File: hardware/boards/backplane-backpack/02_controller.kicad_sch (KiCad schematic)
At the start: 4 parts, among them J10 SWD, U1 STM32C092FCP6

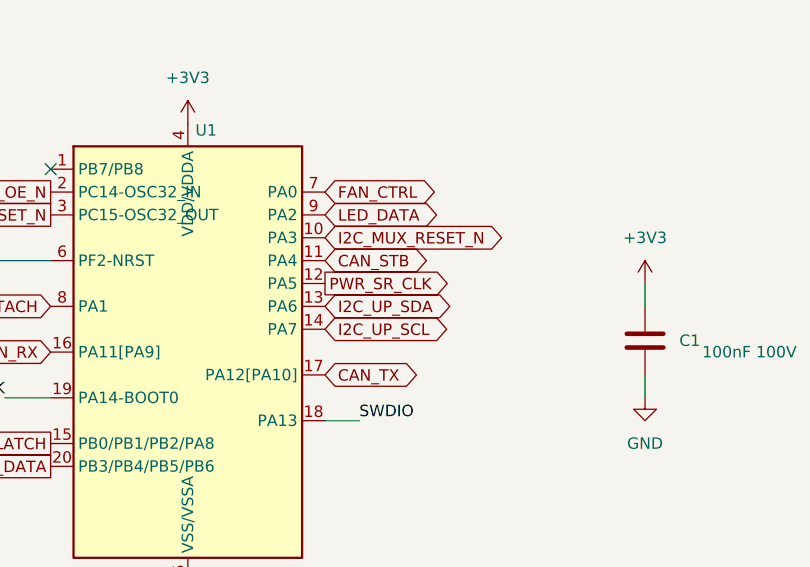
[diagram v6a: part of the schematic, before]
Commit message: feat: replicate slot power switch layouts
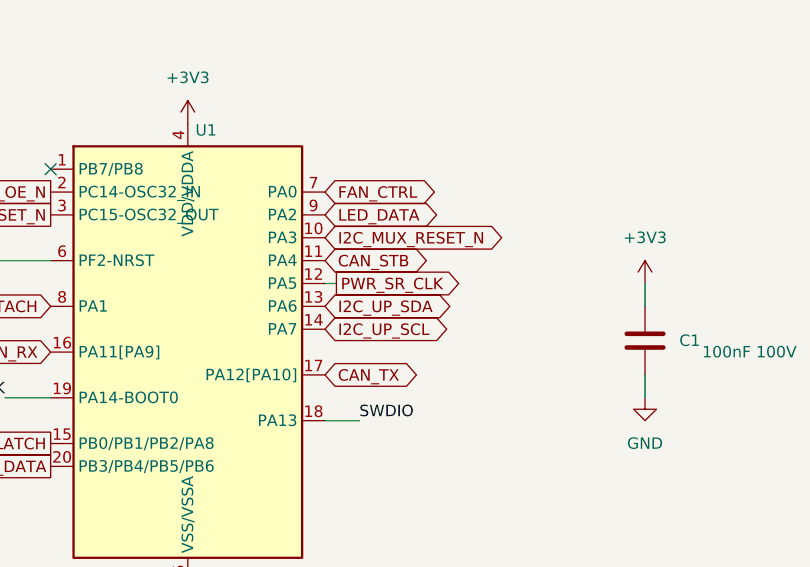
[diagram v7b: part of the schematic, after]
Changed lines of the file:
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@@
+	(wire
+		(pts
+			(xy 118.11 93.98) (xy 116.84 93.98)
+		)
+		(stroke
+			(width 0)
+			(type default)
+		)
+	)
 	(wire
 		(pts
@@
 			)
 			(justify left bottom)
+		)
+	)
+	(global_label "I2C_UP_SCL"
+		(shape bidirectional)
+		(at 116.84 99.06 0)
+		(effects
+			(font
+				(size 1.27 1.27)
+			)
+			(justify left)
+		)
+		(property "Intersheetrefs" "${INTERSHEET_REFS}"
+			(at 116.84 99.06 0)
+			(hide yes)
+			(show_name no)
+			(do_not_autoplace no)
+			(effects
+				(font
+					(size 1.27 1.27)
+				)
+			)
+		)
+	)
+	(global_label "PWR_SR_CLK"
+		(shape output)
+		(at 118.11 93.98 0)
+		(effects
+			(font
+				(size 1.27 1.27)
+			)
+			(justify left)
+		)
+		(property "Intersheetrefs" "${INTERSHEET_REFS}"
+			(at 118.11 93.98 0)
+			(hide yes)
+			(show_name no)
+			(do_not_autoplace no)
+			(effects
+				(font
+					(size 1.27 1.27)
+				)
+			)
+		)
+	)
+	(global_label "I2C_MUX_RESET_N"
+		(shape bidirectional)
+		(at 116.84 88.9 0)
+		(effects
+			(font
+				(size 1.27 1.27)
+			)
+			(justify left)
+		)
+		(property "Intersheetrefs" "${INTERSHEET_REFS}"
+			(at 116.84 88.9 0)
+			(hide yes)
+			(show_name no)
+			(do_not_autoplace no)
+			(effects
+				(font
+					(size 1.27 1.27)
+				)
+			)
+		)
+	)
+	(global_label "I2C_UP_SDA"
+		(shape bidirectional)
+		(at 116.84 96.52 0)
+		(effects
+			(font
+				(size 1.27 1.27)
+			)
+			(justify left)
+		)
+		(property "Intersheetrefs" "${INTERSHEET_REFS}"
+			(at 116.84 96.52 0)
+			(hide yes)
+			(show_name no)
+			(do_not_autoplace no)
+			(effects
+				(font
+					(size 1.27 1.27)
+				)
+			)
 		)
 	)
@@
 		)
 	)
+	(global_label "CAN_RX"
+		(shape bidirectional)
+		(at 86.36 101.6 180)
+		(effects
+			(font
+				(size 1.27 1.27)
+			)
+			(justify right)
+		)
+		(property "Intersheetrefs" "${INTERSHEET_REFS}"
+			(at 86.36 101.6 0)
+			(hide yes)
+			(show_name no)
+			(do_not_autoplace no)
+			(effects
+				(font
+					(size 1.27 1.27)
+				)
+			)
+		)
+	)
 	(global_label "PWR_SR_RESET_N"
 		(shape output)
@@
 		)
 	)
+	(global_label "PWR_SR_CLK"
+		(shape bidirectional)
+		(at 25.4 63.5 0)
+		(effects
+			(font
+				(size 1.27 1.27)
+			)
+			(justify left)
+		)
+		(property "Intersheetrefs" "${INTERSHEET_REFS}"
+			(at 25.4 63.5 0)
+			(hide yes)
+			(show_name no)
+			(do_not_autoplace no)
+			(effects
+				(font
+					(size 1.27 1.27)
+				)
+			)
+		)
+	)
+	(global_label "CAN_STB"
+		(shape bidirectional)
+		(at 116.84 91.44 0)
+		(effects
+			(font
+				(size 1.27 1.27)
+			)
+			(justify left)
+		)
+		(property "Intersheetrefs" "${INTERSHEET_REFS}"
+			(at 116.84 91.44 0)
+			(hide yes)
+			(show_name no)
+			(do_not_autoplace no)
+			(effects
+				(font
+					(size 1.27 1.27)
+				)
+			)
+		)
+	)
+	(global_label "FAN_TACH"
+		(shape bidirectional)
+		(at 86.36 96.52 180)
+		(effects
+			(font
+				(size 1.27 1.27)
+			)
+			(justify right)
+		)
+		(property "Intersheetrefs" "${INTERSHEET_REFS}"
+			(at 86.36 96.52 0)
+			(hide yes)
+			(show_name no)
+			(do_not_autoplace no)
+			(effects
+				(font
+					(size 1.27 1.27)
+				)
+			)
+		)
+	)
+	(global_label "CAN_TX"
+		(shape bidirectional)
+		(at 116.84 104.14 0)
+		(effects
+			(font
+				(size 1.27 1.27)
+			)
+			(justify left)
+		)
+		(property "Intersheetrefs" "${INTERSHEET_REFS}"
+			(at 116.84 104.14 0)
+			(hide yes)
+			(show_name no)
+			(do_not_autoplace no)
+			(effects
+				(font
+					(size 1.27 1.27)
+				)
+			)
+		)
+	)
+	(global_label "LED_DATA"
+		(shape bidirectional)
+		(at 116.84 86.36 0)
+		(effects
+			(font
+				(size 1.27 1.27)
+			)
+			(justify left)
+		)
+		(property "Intersheetrefs" "${INTERSHEET_REFS}"
+			(at 116.84 86.36 0)
+			(hide yes)
+			(show_name no)
+			(do_not_autoplace no)
+			(effects
+				(font
+					(size 1.27 1.27)
+				)
+			)
+		)
+	)
 	(global_label "PWR_SR_DATA"
 		(shape output)
@@
 			(hide yes)
 			(show_name no)
-			(do_not_autoplace no)
-			(effects
-				(font
-					(size 1.27 1.27)
-				)
-			)
-		)
-	)
-	(global_label "I2C_UP_SCL"
-		(shape bidirectional)
-		(at 116.84 99.06 0)
-		(effects
-			(font
-				(size 1.27 1.27)
-			)
-			(justify left)
-		)
-		(property "Intersheetrefs" "${INTERSHEET_REFS}"
-			(at 116.84 99.06 0)
-			(hide yes)
-			(show_name no)
-			(do_not_autoplace no)
-			(effects
-				(font
-					(size 1.27 1.27)
-				)
-			)
-		)
-	)
-	(global_label "PWR_SR_CLK"
-		(shape output)
-		(at 116.84 93.98 0)
-		(effects
-			(font
-				(size 1.27 1.27)
-			)
-			(justify left)
-		)
-		(property "Intersheetrefs" "${INTERSHEET_REFS}"
-			(at 116.84 93.98 0)
-			(hide yes)
-			(show_name no)
-			(do_not_autoplace no)
-			(effects
-				(font
-					(size 1.27 1.27)
-				)
-			)
-		)
-	)
-	(global_label "I2C_MUX_RESET_N"
-		(shape bidirectional)
-		(at 116.84 88.9 0)
-		(effects
-			(font
-				(size 1.27 1.27)
-			)
-			(justify left)
-		)
-		(property "Intersheetrefs" "${INTERSHEET_REFS}"
-			(at 116.84 88.9 0)
-			(hide yes)
-			(show_name no)
-			(do_not_autoplace no)
-			(effects
-				(font
-					(size 1.27 1.27)
-				)
-			)
-		)
-	)
-	(global_label "I2C_UP_SDA"
-		(shape bidirectional)
-		(at 116.84 96.52 0)
-		(effects
-			(font
-				(size 1.27 1.27)
-			)
-			(justify left)
-		)
-		(property "Intersheetrefs" "${INTERSHEET_REFS}"
-			(at 116.84 96.52 0)
-			(hide yes)
-			(show_name no)
-			(do_not_autoplace no)
-			(effects
-				(font
-					(size 1.27 1.27)
-				)
-			)
-		)
-	)
-	(global_label "CAN_RX"
-		(shape bidirectional)
-		(at 86.36 101.6 180)
-		(effects
-			(font
-				(size 1.27 1.27)
-			)
-			(justify right)
-		)
-		(property "Intersheetrefs" "${INTERSHEET_REFS}"
-			(at 86.36 101.6 0)
-			(hide yes)
-			(show_name no)
-			(do_not_autoplace no)
-			(effects
-				(font
-					(size 1.27 1.27)
-				)
-			)
-		)
-	)
-	(global_label "PWR_SR_CLK"
-		(shape bidirectional)
-		(at 25.4 63.5 0)
-		(effects
-			(font
-				(size 1.27 1.27)
-			)
-			(justify left)
-		)
-		(property "Intersheetrefs" "${INTERSHEET_REFS}"
-			(at 25.4 63.5 0)
-			(hide yes)
-			(show_name no)
-			(do_not_autoplace no)
-			(effects
-				(font
-					(size 1.27 1.27)
-				)
-			)
-		)
-	)
-	(global_label "CAN_STB"
-		(shape bidirectional)
-		(at 116.84 91.44 0)
-		(effects
-			(font
-				(size 1.27 1.27)
-			)
-			(justify left)
-		)
-		(property "Intersheetrefs" "${INTERSHEET_REFS}"
-			(at 116.84 91.44 0)
-			(hide yes)
-			(show_name no)
-			(do_not_autoplace no)
-			(effects
-				(font
-					(size 1.27 1.27)
-				)
-			)
-		)
-	)
-	(global_label "FAN_TACH"
-		(shape bidirectional)
-		(at 86.36 96.52 180)
-		(effects
-			(font
-				(size 1.27 1.27)
-			)
-			(justify right)
-		)
-		(property "Intersheetrefs" "${INTERSHEET_REFS}"
-			(at 86.36 96.52 0)
-			(hide yes)
-			(show_name no)
-			(do_not_autoplace no)
-			(effects
-				(font
-					(size 1.27 1.27)
-				)
-			)
-		)
-	)
-	(global_label "CAN_TX"
-		(shape bidirectional)
-		(at 116.84 104.14 0)
-		(effects
-			(font
-				(size 1.27 1.27)
-			)
-			(justify left)
-		)
-		(property "Intersheetrefs" "${INTERSHEET_REFS}"
-			(at 116.84 104.14 0)
-			(hide yes)
-			(show_name no)
-			(do_not_autoplace no)
-			(effects
-				(font
-					(size 1.27 1.27)
-				)
-			)
-		)
-	)
-	(global_label "LED_DATA"
-		(shape bidirectional)
-		(at 116.84 86.36 0)
-		(effects
-			(font
-				(size 1.27 1.27)
-			)
-			(justify left)
-		)
-		(property "Intersheetrefs" "${INTERSHEET_REFS}"
-			(at 116.84 86.36 0)
-			(hide yes)
-			(show_name no)

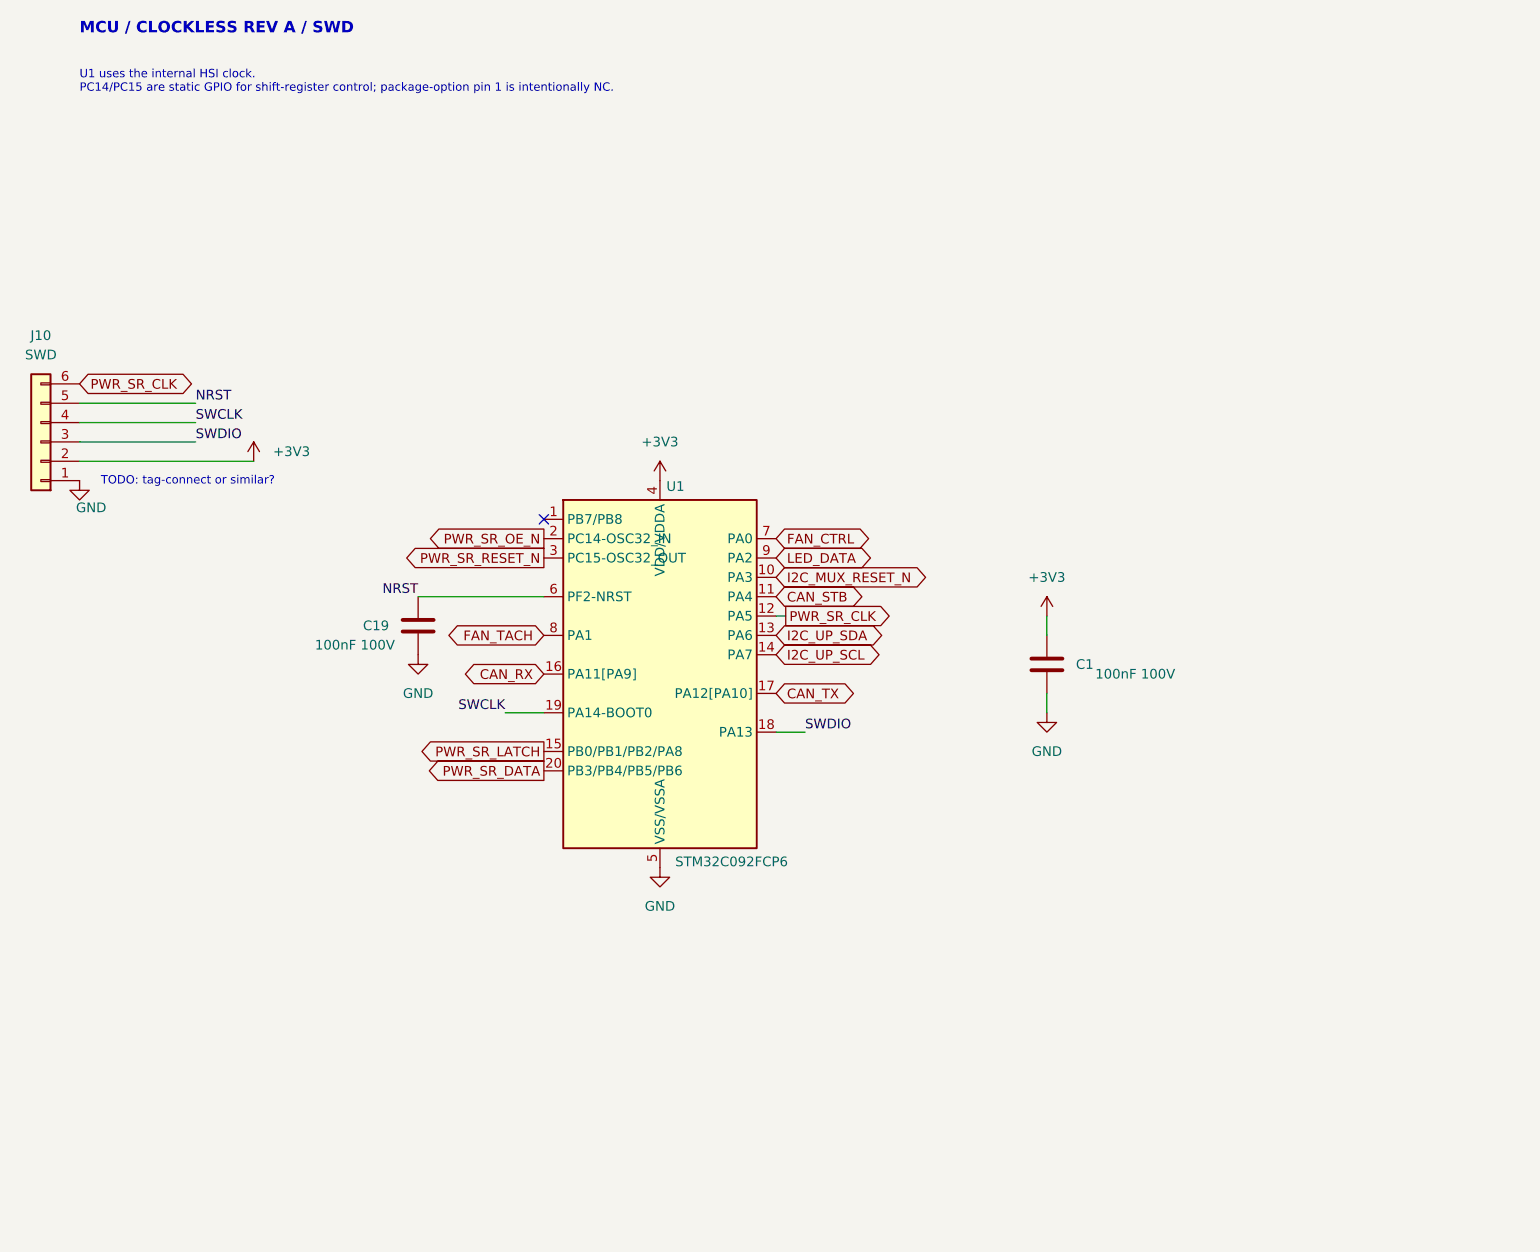
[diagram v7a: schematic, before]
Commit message: Replace slot power shift register with PCA9554
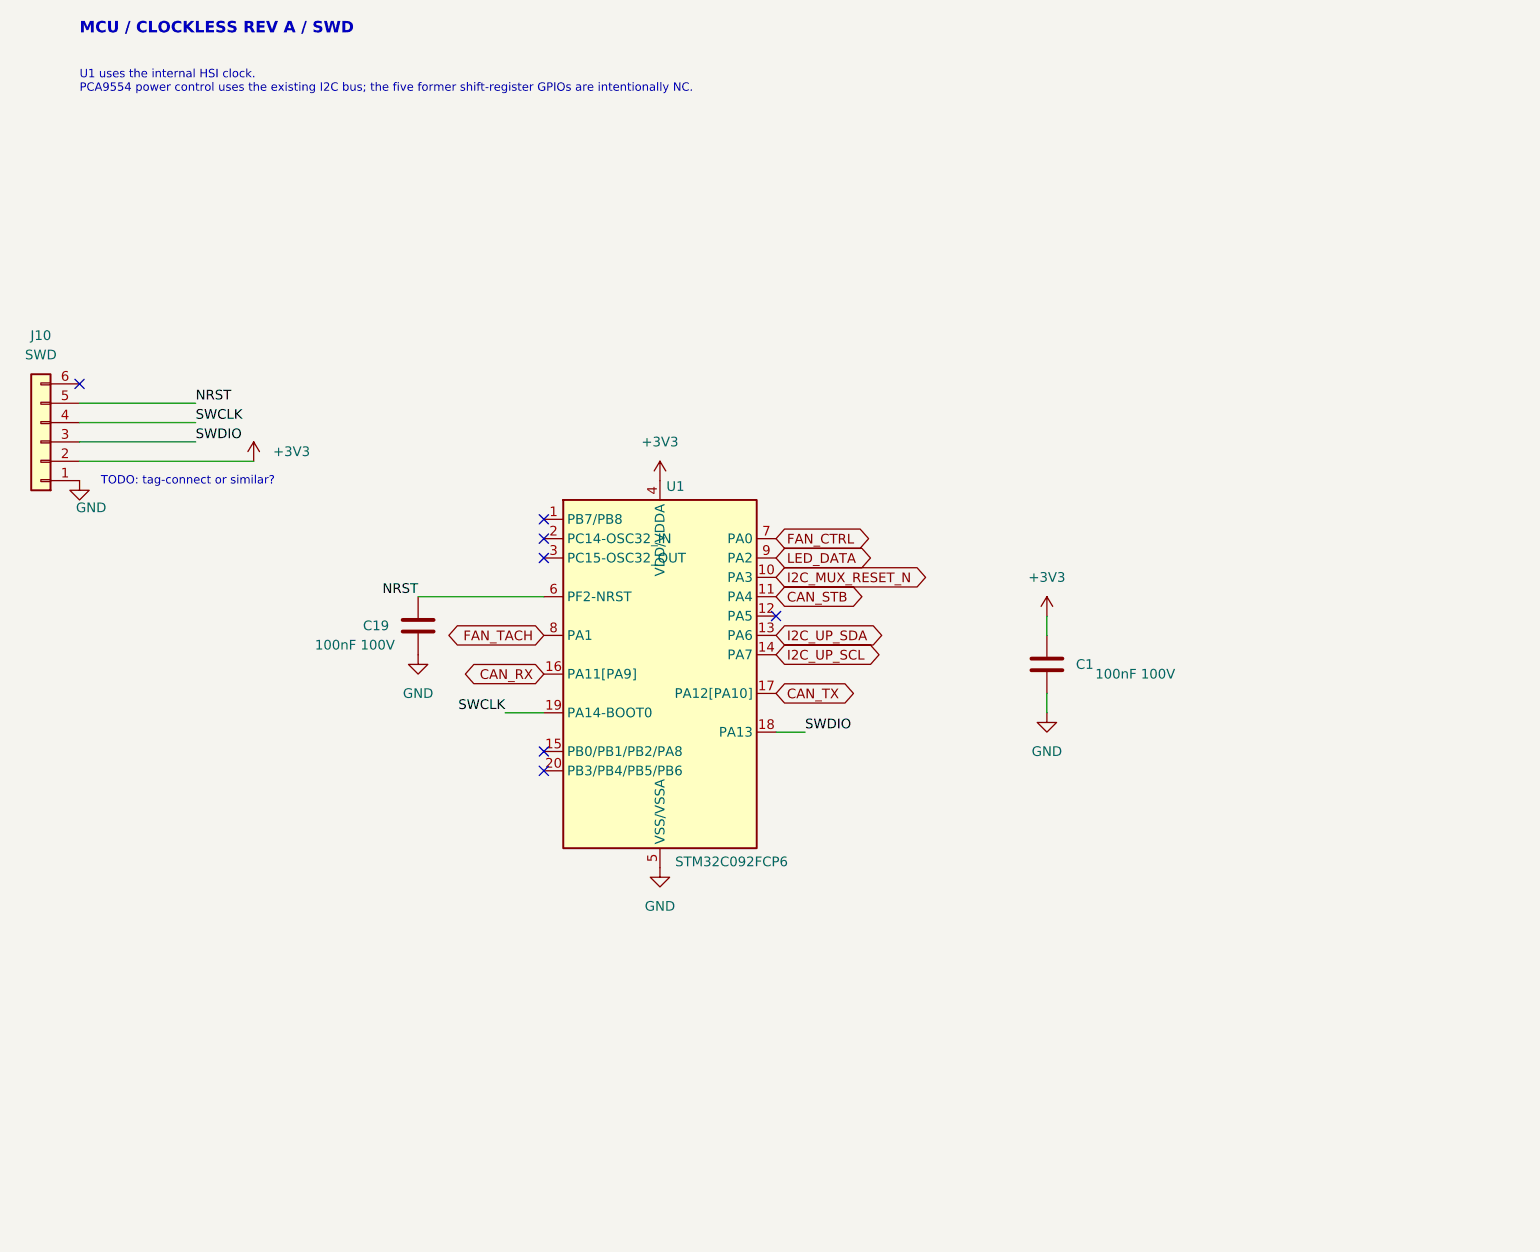
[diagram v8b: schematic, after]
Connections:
- net PWR_SR_CLK: no longer names the net of U1.12 (PA5)
- net PWR_SR_CLK: no longer J10.6 (Pin_6)
- net PWR_SR_DATA: no longer names the net of U1.20 (PB3/PB4/PB5/PB6)
- net PWR_SR_LATCH: no longer names the net of U1.15 (PB0/PB1/PB2/PA8)
- net PWR_SR_OE_N: no longer names the net of U1.2 (PC14-OSC32_IN)
- net PWR_SR_RESET_N: no longer names the net of U1.3 (PC15-OSC32_OUT)
- no-connect marks 1 -> 7
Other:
- note added: "U1 uses the internal HSI clock. PCA9554 power control uses the existing I2C bus; the five former shift-register GPIOs are intentionally NC."
- note removed: "U1 uses the internal HSI clock. PC14/PC15 are static GPIO for shift-register control; package-option pin 1 is intentionally NC."
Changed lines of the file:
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@@
 		)
 	)
-	(text "U1 uses the internal HSI clock.\nPC14/PC15 are static GPIO for shift-register control; package-option pin 1 is intentionally NC."
+	(text "U1 uses the internal HSI clock.\nPCA9554 power control uses the existing I2C bus; the five former shift-register GPIOs are intentionally NC."
 		(exclude_from_sim no)
 		(at 25.4 25.4 0)
@@
 	(wire
 		(pts
-			(xy 118.11 93.98) (xy 116.84 93.98)
-		)
-		(stroke
-			(width 0)
-			(type default)
-		)
-	)
-	(wire
-		(pts
 			(xy 152.4 96.52) (xy 152.4 93.98)
 		)
@@
 		)
 	)
-	(global_label "PWR_SR_CLK"
-		(shape output)
-		(at 118.11 93.98 0)
-		(effects
-			(font
-				(size 1.27 1.27)
-			)
-			(justify left)
-		)
-		(property "Intersheetrefs" "${INTERSHEET_REFS}"
-			(at 118.11 93.98 0)
-			(hide yes)
-			(show_name no)
-			(do_not_autoplace no)
-			(effects
-				(font
-					(size 1.27 1.27)
-				)
-			)
-		)
-	)
 	(global_label "I2C_MUX_RESET_N"
 		(shape bidirectional)
@@
 		)
 	)
-	(global_label "PWR_SR_OE_N"
-		(shape output)
-		(at 86.36 83.82 180)
+	(global_label "CAN_RX"
+		(shape bidirectional)
+		(at 86.36 101.6 180)
 		(effects
 			(font
@@
 		)
 		(property "Intersheetrefs" "${INTERSHEET_REFS}"
-			(at 86.36 83.82 0)
-			(hide yes)
-			(show_name no)
-			(do_not_autoplace no)
-			(effects
-				(font
-					(size 1.27 1.27)
-				)
-			)
-		)
-	)
-	(global_label "CAN_RX"
-		(shape bidirectional)
-		(at 86.36 101.6 180)
+			(at 86.36 101.6 0)
+			(hide yes)
+			(show_name no)
+			(do_not_autoplace no)
+			(effects
+				(font
+					(size 1.27 1.27)
+				)
+			)
+		)
+	)
+	(global_label "CAN_STB"
+		(shape bidirectional)
+		(at 116.84 91.44 0)
+		(effects
+			(font
+				(size 1.27 1.27)
+			)
+			(justify left)
+		)
+		(property "Intersheetrefs" "${INTERSHEET_REFS}"
+			(at 116.84 91.44 0)
+			(hide yes)
+			(show_name no)
+			(do_not_autoplace no)
+			(effects
+				(font
+					(size 1.27 1.27)
+				)
+			)
+		)
+	)
+	(global_label "FAN_TACH"
+		(shape bidirectional)
+		(at 86.36 96.52 180)
 		(effects
 			(font
@@
 		)
 		(property "Intersheetrefs" "${INTERSHEET_REFS}"
-			(at 86.36 101.6 0)
-			(hide yes)
-			(show_name no)
-			(do_not_autoplace no)
-			(effects
-				(font
-					(size 1.27 1.27)
-				)
-			)
-		)
-	)
-	(global_label "PWR_SR_RESET_N"
-		(shape output)
-		(at 86.36 86.36 180)
-		(effects
-			(font
-				(size 1.27 1.27)
-			)
-			(justify right)
-		)
-		(property "Intersheetrefs" "${INTERSHEET_REFS}"
-			(at 86.36 86.36 0)
-			(hide yes)
-			(show_name no)
-			(do_not_autoplace no)
-			(effects
-				(font
-					(size 1.27 1.27)
-				)
-			)
-		)
-	)
-	(global_label "PWR_SR_LATCH"
-		(shape output)
-		(at 86.36 111.76 180)
-		(effects
-			(font
-				(size 1.27 1.27)
-			)
-			(justify right)
-		)
-		(property "Intersheetrefs" "${INTERSHEET_REFS}"
-			(at 86.36 111.76 0)
-			(hide yes)
-			(show_name no)
-			(do_not_autoplace no)
-			(effects
-				(font
-					(size 1.27 1.27)
-				)
-			)
-		)
-	)
-	(global_label "PWR_SR_CLK"
-		(shape bidirectional)
-		(at 25.4 63.5 0)
-		(effects
-			(font
-				(size 1.27 1.27)
-			)
-			(justify left)
-		)
-		(property "Intersheetrefs" "${INTERSHEET_REFS}"
-			(at 25.4 63.5 0)
-			(hide yes)
-			(show_name no)
-			(do_not_autoplace no)
-			(effects
-				(font
-					(size 1.27 1.27)
-				)
-			)
-		)
-	)
-	(global_label "CAN_STB"
-		(shape bidirectional)
-		(at 116.84 91.44 0)
-		(effects
-			(font
-				(size 1.27 1.27)
-			)
-			(justify left)
-		)
-		(property "Intersheetrefs" "${INTERSHEET_REFS}"
-			(at 116.84 91.44 0)
-			(hide yes)
-			(show_name no)
-			(do_not_autoplace no)
-			(effects
-				(font
-					(size 1.27 1.27)
-				)
-			)
-		)
-	)
-	(global_label "FAN_TACH"
-		(shape bidirectional)
-		(at 86.36 96.52 180)
-		(effects
-			(font
-				(size 1.27 1.27)
-			)
-			(justify right)
-		)
-		(property "Intersheetrefs" "${INTERSHEET_REFS}"
 			(at 86.36 96.52 0)
 			(hide yes)
@@
 		)
 	)
-	(global_label "PWR_SR_DATA"
-		(shape output)
-		(at 86.36 114.3 180)
-		(effects
-			(font
-				(size 1.27 1.27)
-			)
-			(justify right)
-		)
-		(property "Intersheetrefs" "${INTERSHEET_REFS}"
-			(at 86.36 114.3 0)
-			(hide yes)
-			(show_name no)
-			(do_not_autoplace no)
-			(effects
-				(font
-					(size 1.27 1.27)
-				)
-			)
-		)
-	)
 	(global_label "FAN_CTRL"
 		(shape bidirectional)
@@
 		)
 	)
+		(no_connect
+		(at 116.84 93.98)
+	)
+	(no_connect
+		(at 86.36 83.82)
+	)
+	(no_connect
+		(at 86.36 86.36)
+	)
+	(no_connect
+		(at 86.36 111.76)
+	)
+	(no_connect
+		(at 25.4 63.5)
+	)
+	(no_connect
+		(at 86.36 114.3)
+	)
 	(symbol
